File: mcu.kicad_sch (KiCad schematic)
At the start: 46 parts, among them J3 SWITCHES, J4 Debug, J5 USB_B, J6 SPI UP, J7 SPI DOWN, SW1 ERASE, SW2 RESET, U4 M95010, U5 SAM4S2A, U6 AP7381-33Y-13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

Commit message: changes for layout
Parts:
- added J8: USB_B, Connector_USB:USB_Micro-B_Amphenol_10118194_Horizontal, symbol Connector:USB_B
- added R44: 0, Resistor_SMD:R_0603_1608Metric_Pad0.98x0.95mm_HandSolder, symbol Device:R
- J4: footprint (none) -> Connector_PinHeader_2.54mm:PinHeader_1x04_P2.54mm_Vertical
- J5: footprint Connector_USB:USB_B_TE_5787834_Vertical -> Connector_USB:USB_Micro-B_Amphenol_10118194_Horizontal; Digikey A121598-ND -> 609-4618-1-ND
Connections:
- net +5V: now also J8.1 (VBUS), R44.2; no longer J5.1 (VBUS)
- net GND: now also C24.2, FB24.2, J8.4 (GND), J8.5 (Shield)
- net OUT_0: now also U5.24 (PA7); no longer U5.9 (PA17)
- net OUT_1: now also U5.23 (PA8); no longer U5.10 (PA18)
- net OUT_2: now also U5.15 (PA15); no longer U5.11 (PA19)
- net OUT_3: now also U5.14 (PA16); no longer U5.12 (PA20)
- net OUT_4: now also U5.12 (PA20); no longer U5.14 (PA16)
- net OUT_5: now also U5.11 (PA19); no longer U5.15 (PA15)
- net OUT_6: now also U5.10 (PA18); no longer U5.23 (PA8)
- net OUT_7: now also U5.9 (PA17); no longer U5.24 (PA7)
- net USB-: now reaches J5.2 (D-), R32.2
- net USB+: now reaches J5.3 (D+), R33.2
- new net: J5.1 (VBUS), R44.1

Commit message: added some part numbers
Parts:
- U4: Digikey (none) -> 497-8672-1-ND
- U5: Digikey (none) -> ATSAM4S2AB-ANR-CT-ND
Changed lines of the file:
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@@
+      (effects (font (size 1.27 1.27)) hide)
+    )
+    (property "Digikey" "ATSAM4S2AB-ANR-CT-ND" (id 4) (at 129.54 118.11 0)
       (effects (font (size 1.27 1.27)) hide)
     )
@@
       (effects (font (size 1.27 1.27)) hide)
     )
+    (property "Digikey" "ATSAM4S2AB-ANR-CT-ND" (id 4) (at 129.54 118.11 0)
+      (effects (font (size 1.27 1.27)) hide)
+    )
     (pin "1")
     (pin "13")
@@
       (effects (font (size 1.27 1.27)) hide)
     )
+    (property "Digikey" "497-8672-1-ND" (id 4) (at 60.96 48.26 0)
+      (effects (font (size 1.27 1.27)) hide)
+    )

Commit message: add copyright notices
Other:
- note added: "Copyright (C) 2023"
- note added: "Jonathan Bagg"
- note added: "SOLAR CONTROLLER 2023 - MCU"
- note added: "See https://creativecommons.org/licenses/by-nc-sa/4.0/"
- note added: "v1"
- moved on the sheet: C30, C31, C32, C33, C34, C35, C36, C37, C38, U5A

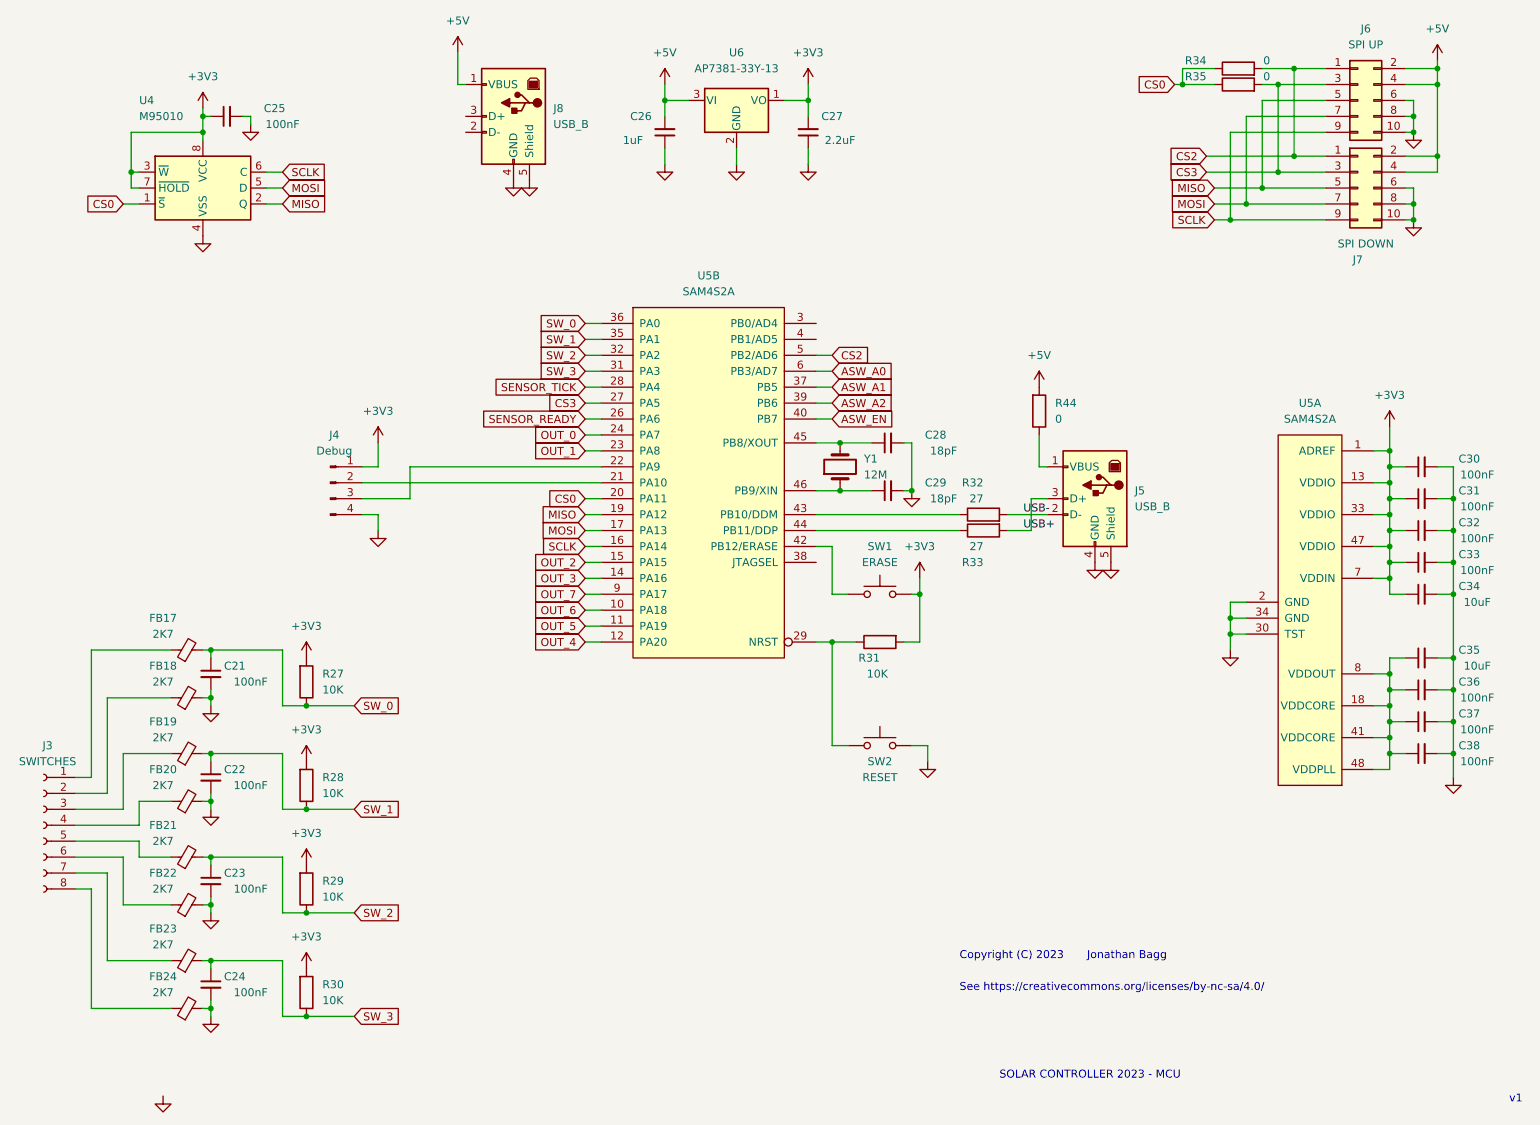
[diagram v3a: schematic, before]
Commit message: AC couple LMT01 signal conditioning and add gain
The difference circuit U3A was DC coupled and so could not
have gain.  Unit gain was only good for sensors up to 15m of
cat-5.
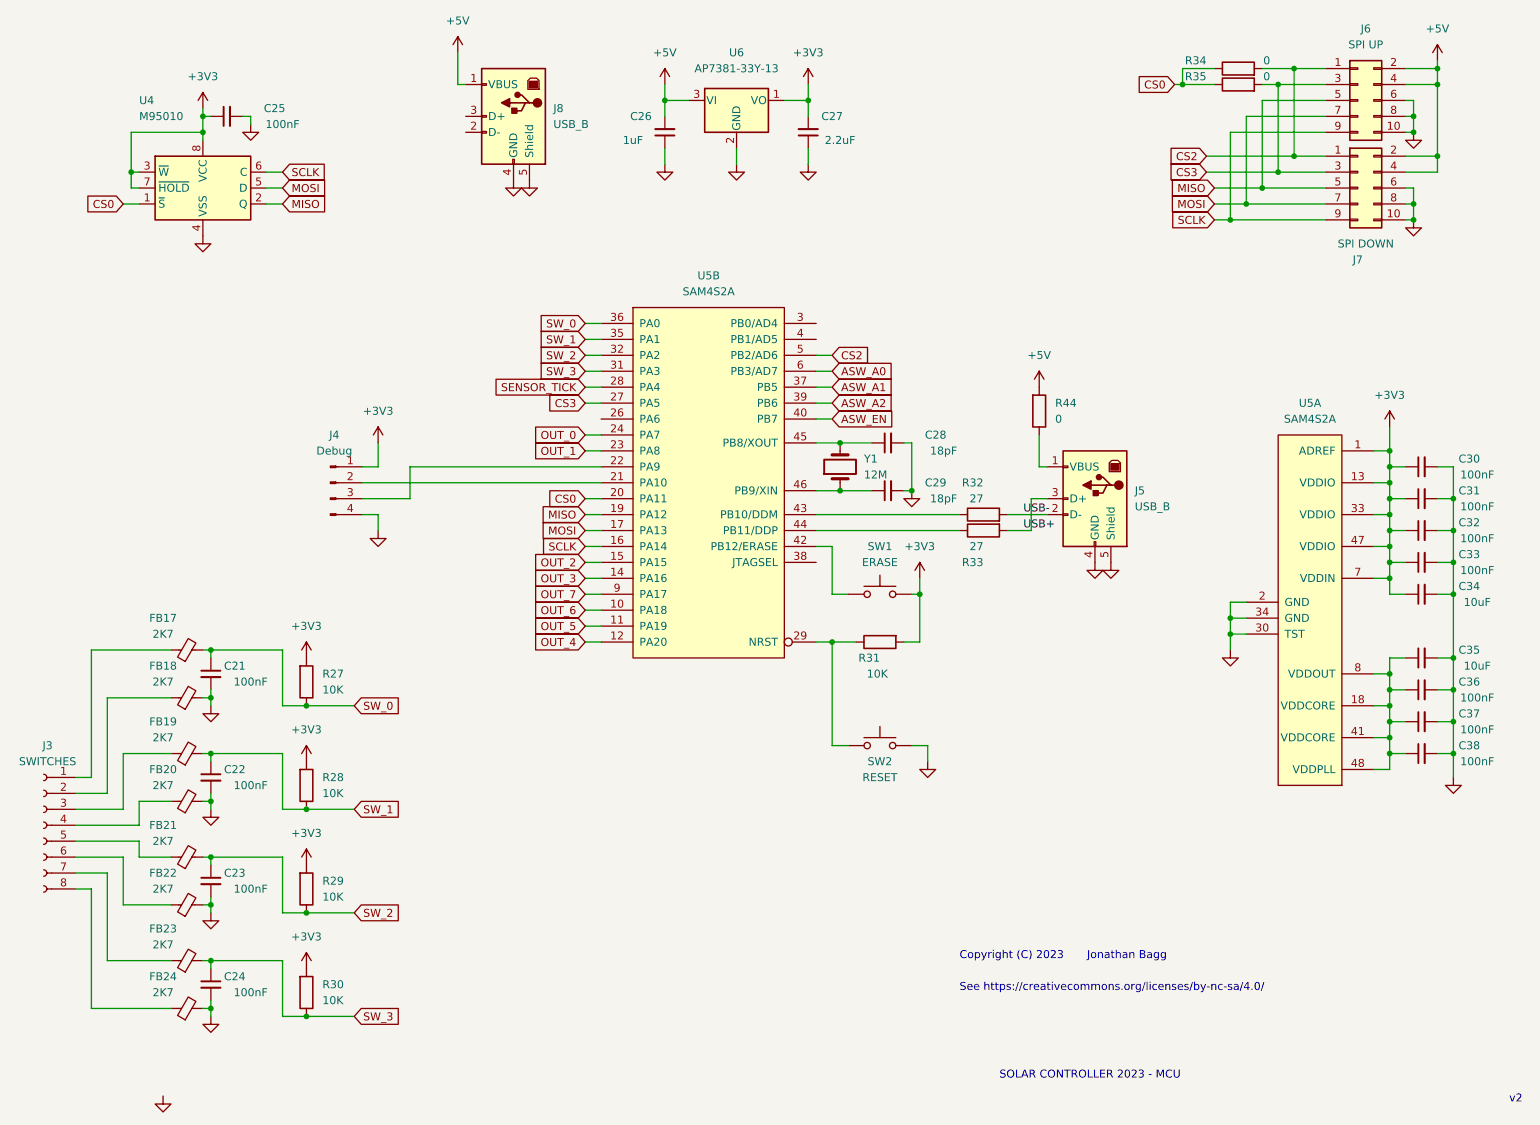
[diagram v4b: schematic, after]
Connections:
- net SENSOR_READY: no longer names the net of U5.26 (PA6)
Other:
- note added: "v2"
- note removed: "v1"
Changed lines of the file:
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@@
-    (stroke (width 0) (type default) (color 0 0 0 0))
-  )
-  (wire (pts (xy 121.92 85.09) (xy 124.46 85.09))
     (stroke (width 0) (type default) (color 0 0 0 0))
   )
@@
     (effects (font (size 1.27 1.27)) (justify left bottom))
   )
-  (text "v1" (at 269.24 194.31 0)
+  (text "v2" (at 269.24 194.31 0)
     (effects (font (size 1.27 1.27)) (justify left bottom))
   )
@@
       (effects (font (size 1.27 1.27)) (justify right) hide)
     )
-  )
-  (global_label "SENSOR_READY" (shape input) (at 121.92 85.09 180) (fields_autoplaced)
-    (effects (font (size 1.27 1.27)) (justify right))
-    (property "Intersheet References" "${INTERSHEET_REFS}" (id 0) (at 105.174 85.0106 0)
-      (effects (font (size 1.27 1.27)) (justify right) hide)
-    )

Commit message: replace sensor wire esd caps with TVSs
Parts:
- U6: footprint Package_TO_SOT_SMD:SOT-89-3 -> Package_TO_SOT_SMD:SOT-89-3-JB
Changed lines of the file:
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@@
     (property "Reference" "U6" (id 0) (at 146.05 26.67 0))
     (property "Value" "AP7381-33Y-13" (id 1) (at 146.05 29.21 0))
-    (property "Footprint" "Package_TO_SOT_SMD:SOT-89-3" (id 2) (at 146.05 28.575 0)
+    (property "Footprint" "Package_TO_SOT_SMD:SOT-89-3-JB" (id 2) (at 146.05 28.575 0)
       (effects (font (size 1.27 1.27) italic) hide)
     )

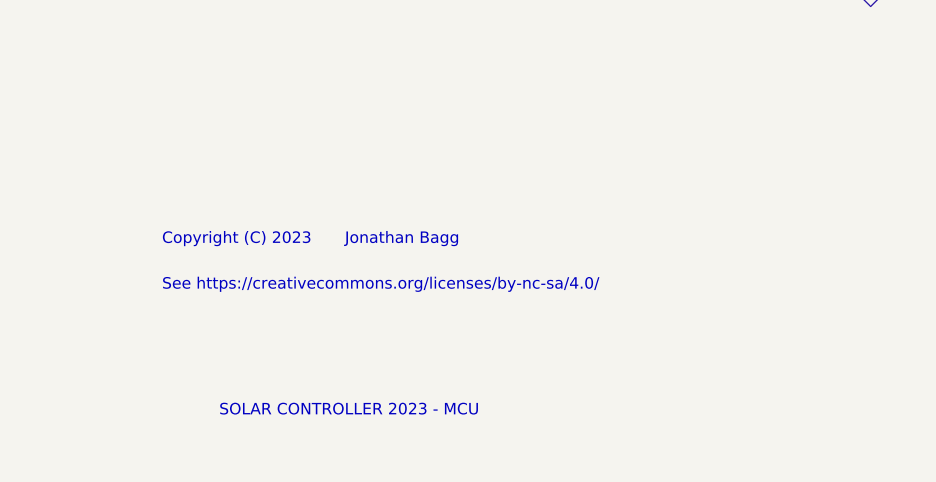
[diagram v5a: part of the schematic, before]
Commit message: add github link to title block and print schematic pdf
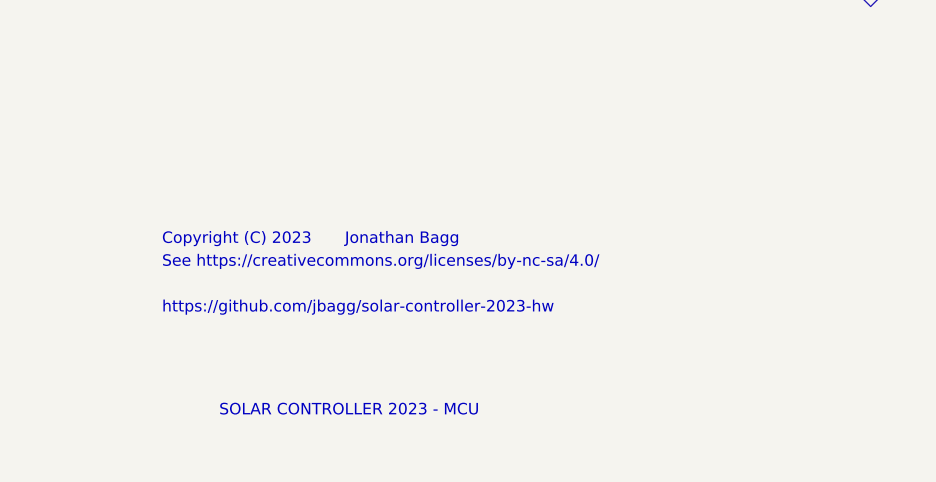
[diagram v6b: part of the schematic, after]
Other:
- note added: "https://github.com/jbagg/solar-controller-2023-hw"
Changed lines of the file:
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@@
   )
   (text "See https://creativecommons.org/licenses/by-nc-sa/4.0/"
-    (at 181.61 176.53 0)
+    (at 181.61 173.99 0)
     (effects (font (size 1.27 1.27)) (justify left bottom))
   )
@@
     (effects (font (size 1.27 1.27)) (justify left bottom))
   )
+  (text "https://github.com/jbagg/solar-controller-2023-hw" (at 181.61 179.07 0)
+    (effects (font (size 1.27 1.27)) (justify left bottom))
+  )
